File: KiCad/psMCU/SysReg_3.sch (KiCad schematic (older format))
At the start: 10 parts

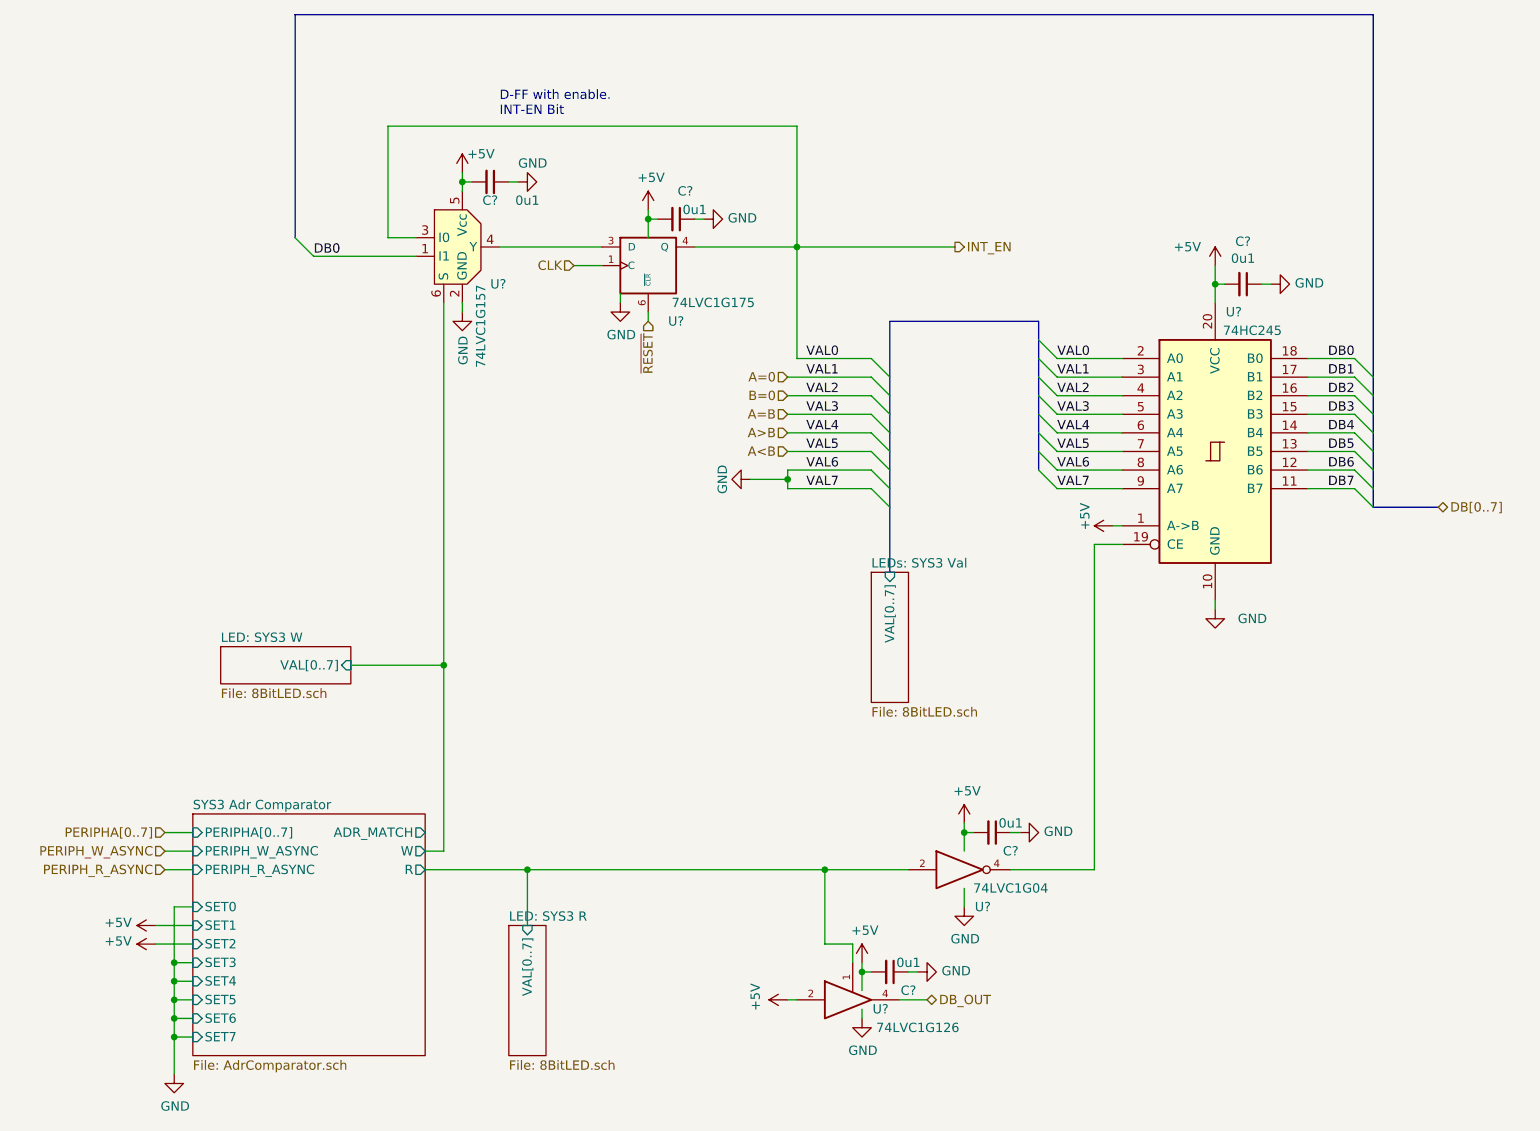
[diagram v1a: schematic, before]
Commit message: First ERC pass
    All unconnects solved, need to inspect Tristate errors.
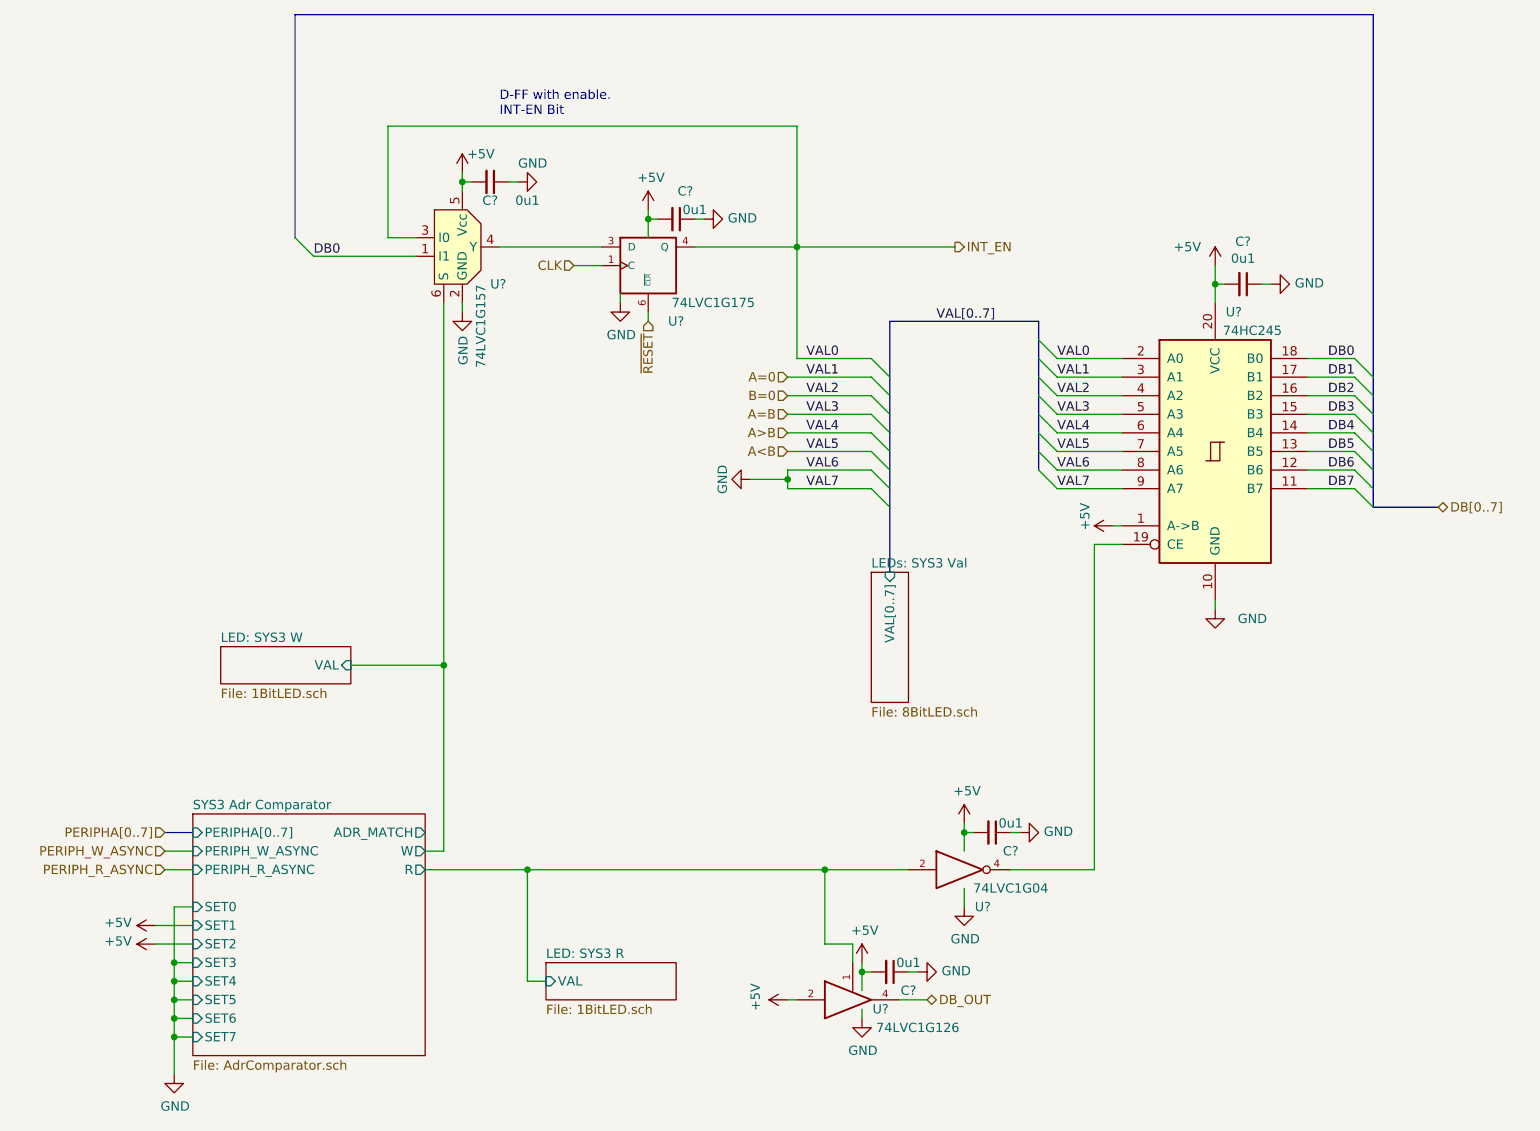
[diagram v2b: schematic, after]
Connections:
- net LED: SYS3 R/VAL[0..7] renamed LED: SYS3 R/VAL
- net LED: SYS3 W/VAL[0..7] renamed LED: SYS3 W/VAL
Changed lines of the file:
@@
 $Descr A4 11693 8268
 encoding utf-8
-Sheet 160 209
+Sheet 185 207
 Title "psMCU"
 Date ""
@@
 Wire Wire Line
 	6250 5550 6700 5550
-$Sheet
-S 3000 4350 700  200
-U 60491F62
-F0 "LED: SYS3 W" 50
-F1 "8BitLED.sch" 50
-F2 "VAL[0..7]" I R 3700 4450 50
-$EndSheet
-$Sheet
-S 4550 5850 200  700
-U 60494872
-F0 "LED: SYS3 R" 50
-F1 "8BitLED.sch" 50
-F2 "VAL[0..7]" I T 4650 5850 50
-$EndSheet
-Wire Wire Line
-	4650 5850 4650 5550
 Wire Wire Line
 	4650 5550 6250 5550
@@
 PERIPH_R_ASYNC
 Wire Wire Line
-	2700 5350 2850 5350
-Wire Wire Line
 	2700 5450 2850 5450
 Wire Wire Line
@@
 	4100 5550 4650 5550
 Connection ~ 4650 5550
+Wire Bus Line
+	2850 5350 2700 5350
+$Sheet
+S 4750 6050 700  200
+U 6053C227
+F0 "LED: SYS3 R" 50
+F1 "1BitLED.sch" 50
+F2 "VAL" I L 4750 6150 50
+$EndSheet
+Wire Wire Line
+	4650 6150 4750 6150
+Wire Wire Line
+	4650 5550 4650 6150
+$Sheet
+S 3000 4350 700  200
+U 605425EC
+F0 "LED: SYS3 W" 50
+F1 "1BitLED.sch" 50
+F2 "VAL" I R 3700 4450 50
+$EndSheet
 Wire Bus Line
 	7400 2600 7400 3400
@@
 Wire Bus Line
 	9200 950  9200 3600
+Text Label 6850 2600 0    50   ~ 0
+VAL[0..7]
 $EndSCHEMATC

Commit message: Added some footprints, small optimisations
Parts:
- U?: footprint (none) -> Package_TO_SOT_SMD:SOT-353_SC-70-5
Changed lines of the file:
@@
 F 0 "U?" H 7100 5350 50  0000 C CNN
 F 1 "74LVC1G04" H 7250 5450 50  0000 C CNN
-F 2 "" H 7000 5550 50  0001 C CNN
+F 2 "Package_TO_SOT_SMD:SOT-353_SC-70-5" H 7000 5550 50  0001 C CNN
 F 3 "http://www.ti.com/lit/sg/scyt129e/scyt129e.pdf" H 7000 5550 50  0001 C CNN
 	1    7000 5550

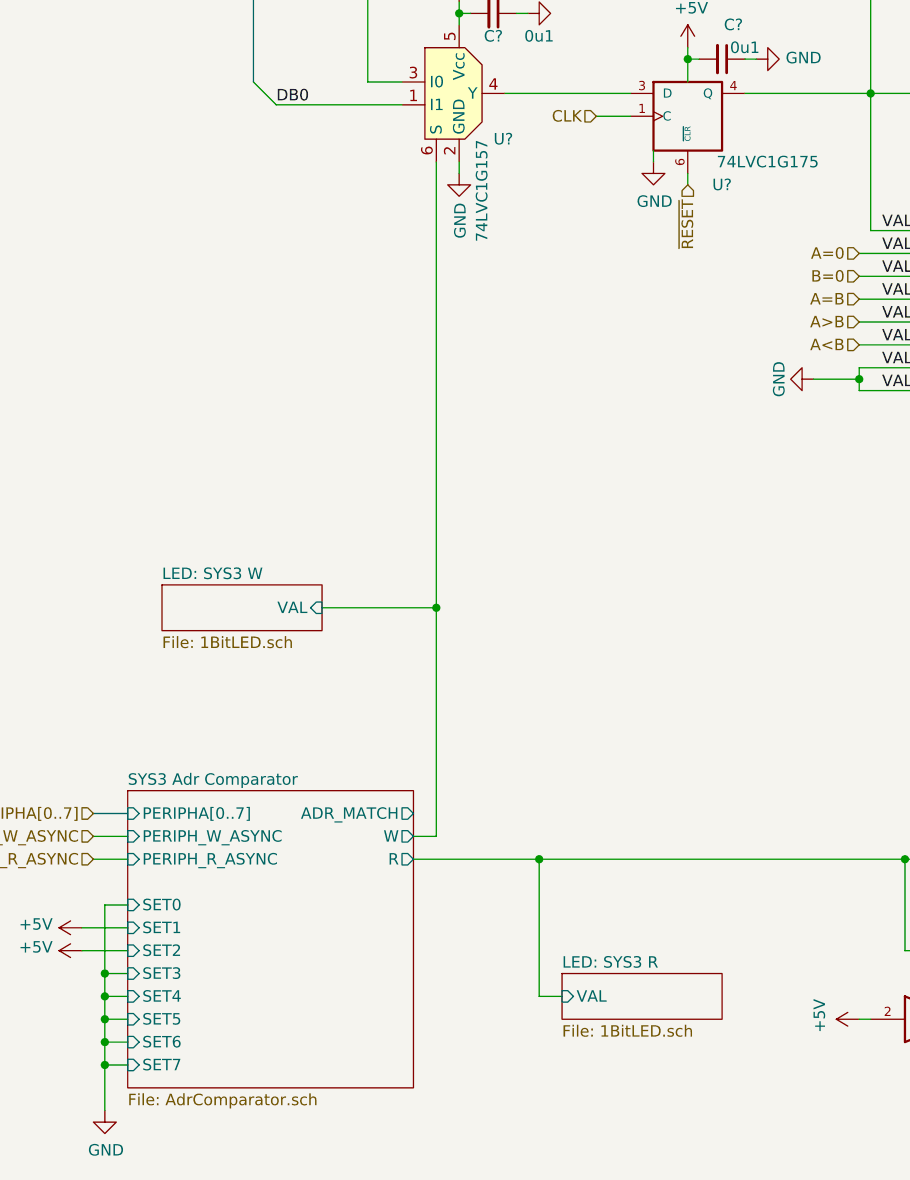
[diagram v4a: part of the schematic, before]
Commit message: Removed Single LED sheets
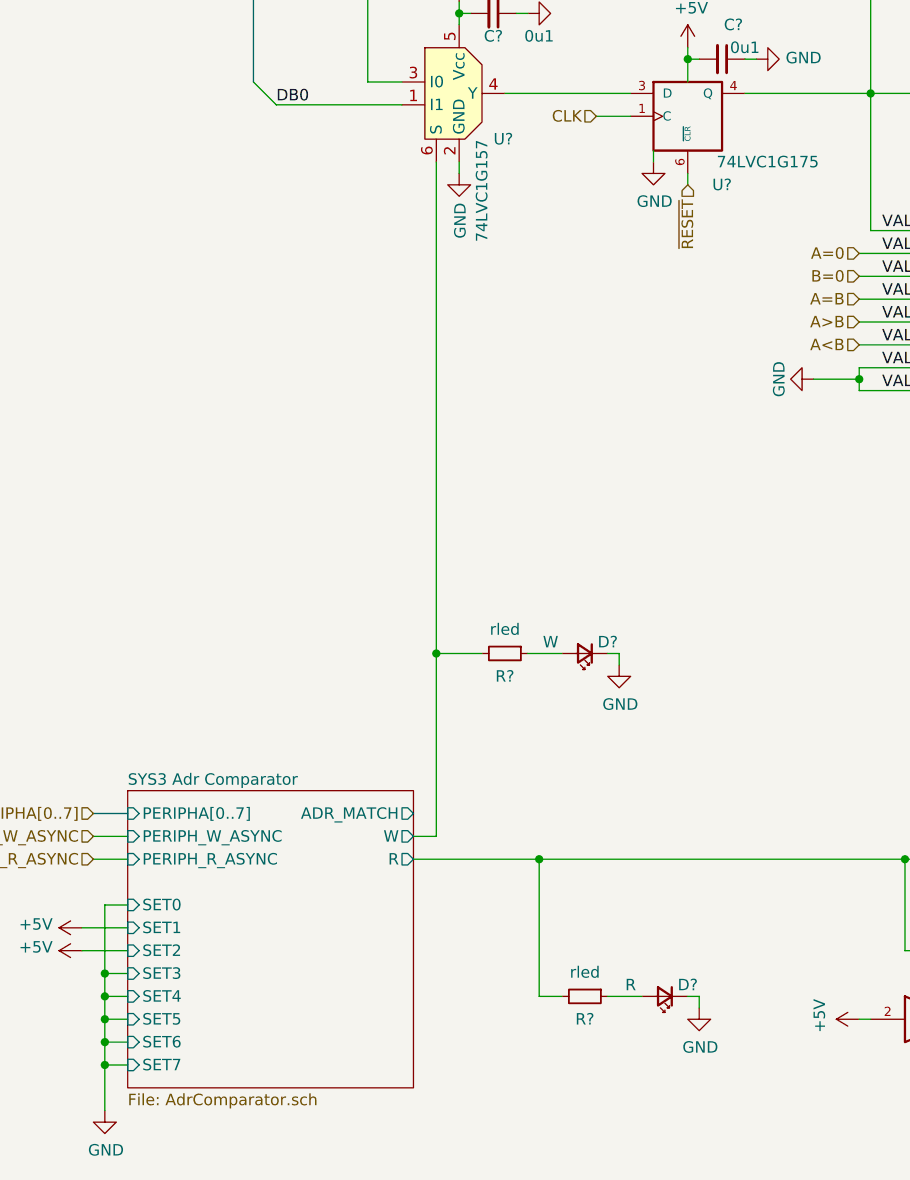
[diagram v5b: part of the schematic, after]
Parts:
- added D?: R, Diode_SMD:D_0603_1608Metric, symbol Device:LED_Small
- added D?: W, Diode_SMD:D_0603_1608Metric, symbol Device:LED_Small
- added R? (x2): rled, Resistor_SMD:R_0603_1608Metric, symbol Device:R_Small
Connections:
- net GND: now also D?.1 (K), D?.1 (K)
- net LED: SYS3 R/VAL renamed SYS3 Adr Comparator/R
- net SYS3 Adr Comparator/R: now also R?.2
- net LED: SYS3 W/VAL renamed SYS3 Adr Comparator/W
- net SYS3 Adr Comparator/W: now also R?.2
- new net: D?.2 (A), R?.1 (x2)

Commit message: First Schematic Draft done.
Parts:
- C370, C371, C372, C373, C374: renamed from C?; footprint Capacitor_SMD:C_0603_1608Metric -> NoRef_Footprints:C_0603_1608Metric_NoRef
- D390, D391: renamed from D?; footprint Diode_SMD:D_0603_1608Metric -> NoRef_Footprints:D_0603_1608Metric_NoRef
- R422, R423: renamed from R?; footprint Resistor_SMD:R_0603_1608Metric -> NoRef_Footprints:R_0603_1608Metric
- gave numbers to parts that had none: 5
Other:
- note added: "Interrupt EN"
- note added: "RAM Page"
- note removed: "D-FF with enable. \nINT-EN Bit"

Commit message: Small improvements.
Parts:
- renumbered C370 to C368, C371 to C369, C372 to C370, C373 to C371, C374 to C372, U354 to U352, U355 to U353, U356 to U354, U357 to U355, U358 to U356
